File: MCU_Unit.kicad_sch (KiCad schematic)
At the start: 35 parts, among them J401 Solder Holes 4x1 2.54mm 22AWG, J402 Conn_ARM_SWD_TagConnect_TC203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, J403 Solder Wire Pad 1,5x3mm, J404 Solder Wire Pad 1,5x3mm, J405 Solder Wire Pad 1,5x3mm, J406 Solder Wire Pad 1,5x3mm, SW401 KMR232NG ULC, SW402 KMR232NG ULC, SW403 CAS-D20A1, SW404 KMR232NG ULC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

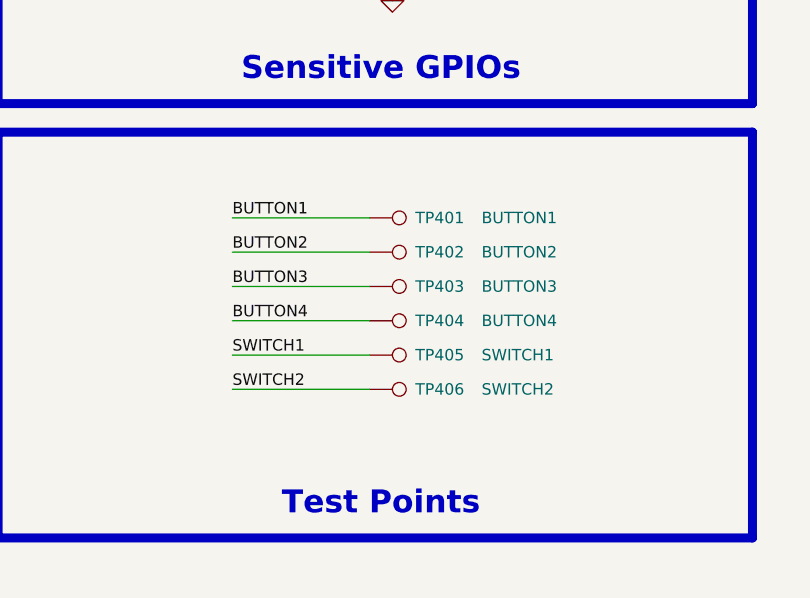
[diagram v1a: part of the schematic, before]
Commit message: Added PCB frame for assembly, almost finished auto-review, only MCU and motors left
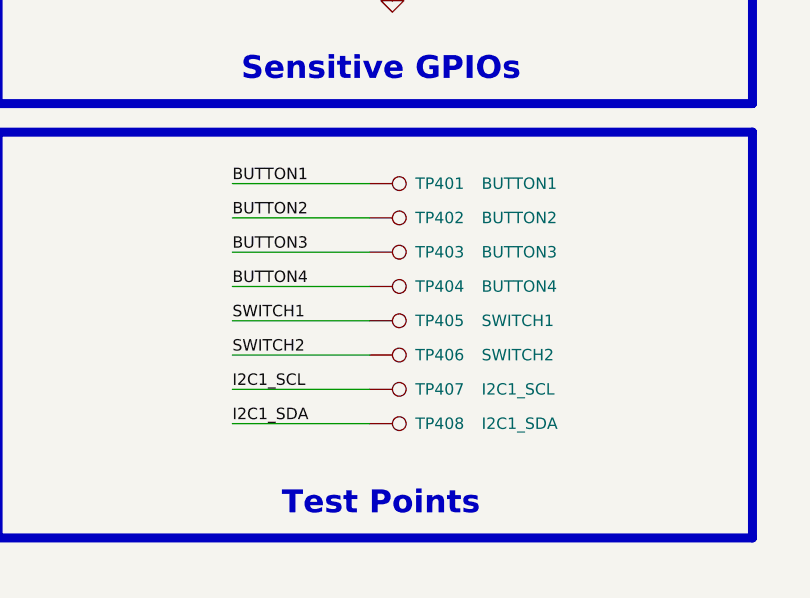
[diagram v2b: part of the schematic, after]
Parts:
- added TP407: I2C1_SCL, 0_Plume:TestPoint_Pad_D0.75mm_Front, symbol Connector:TestPoint
- added TP408: I2C1_SDA, 0_Plume:TestPoint_Pad_D0.75mm_Front, symbol Connector:TestPoint
- TP401, TP402, TP403, TP404, TP405, TP406: footprint 0_Plume:TestPoint_Pad_D0.5mm_Back -> 0_Plume:TestPoint_Pad_D0.5mm_Front
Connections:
- net I2C1_SCL: now also TP407.1
- net I2C1_SDA: now also TP408.1
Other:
- moved on the sheet: TP401, TP402, TP403, TP404, TP405, TP406

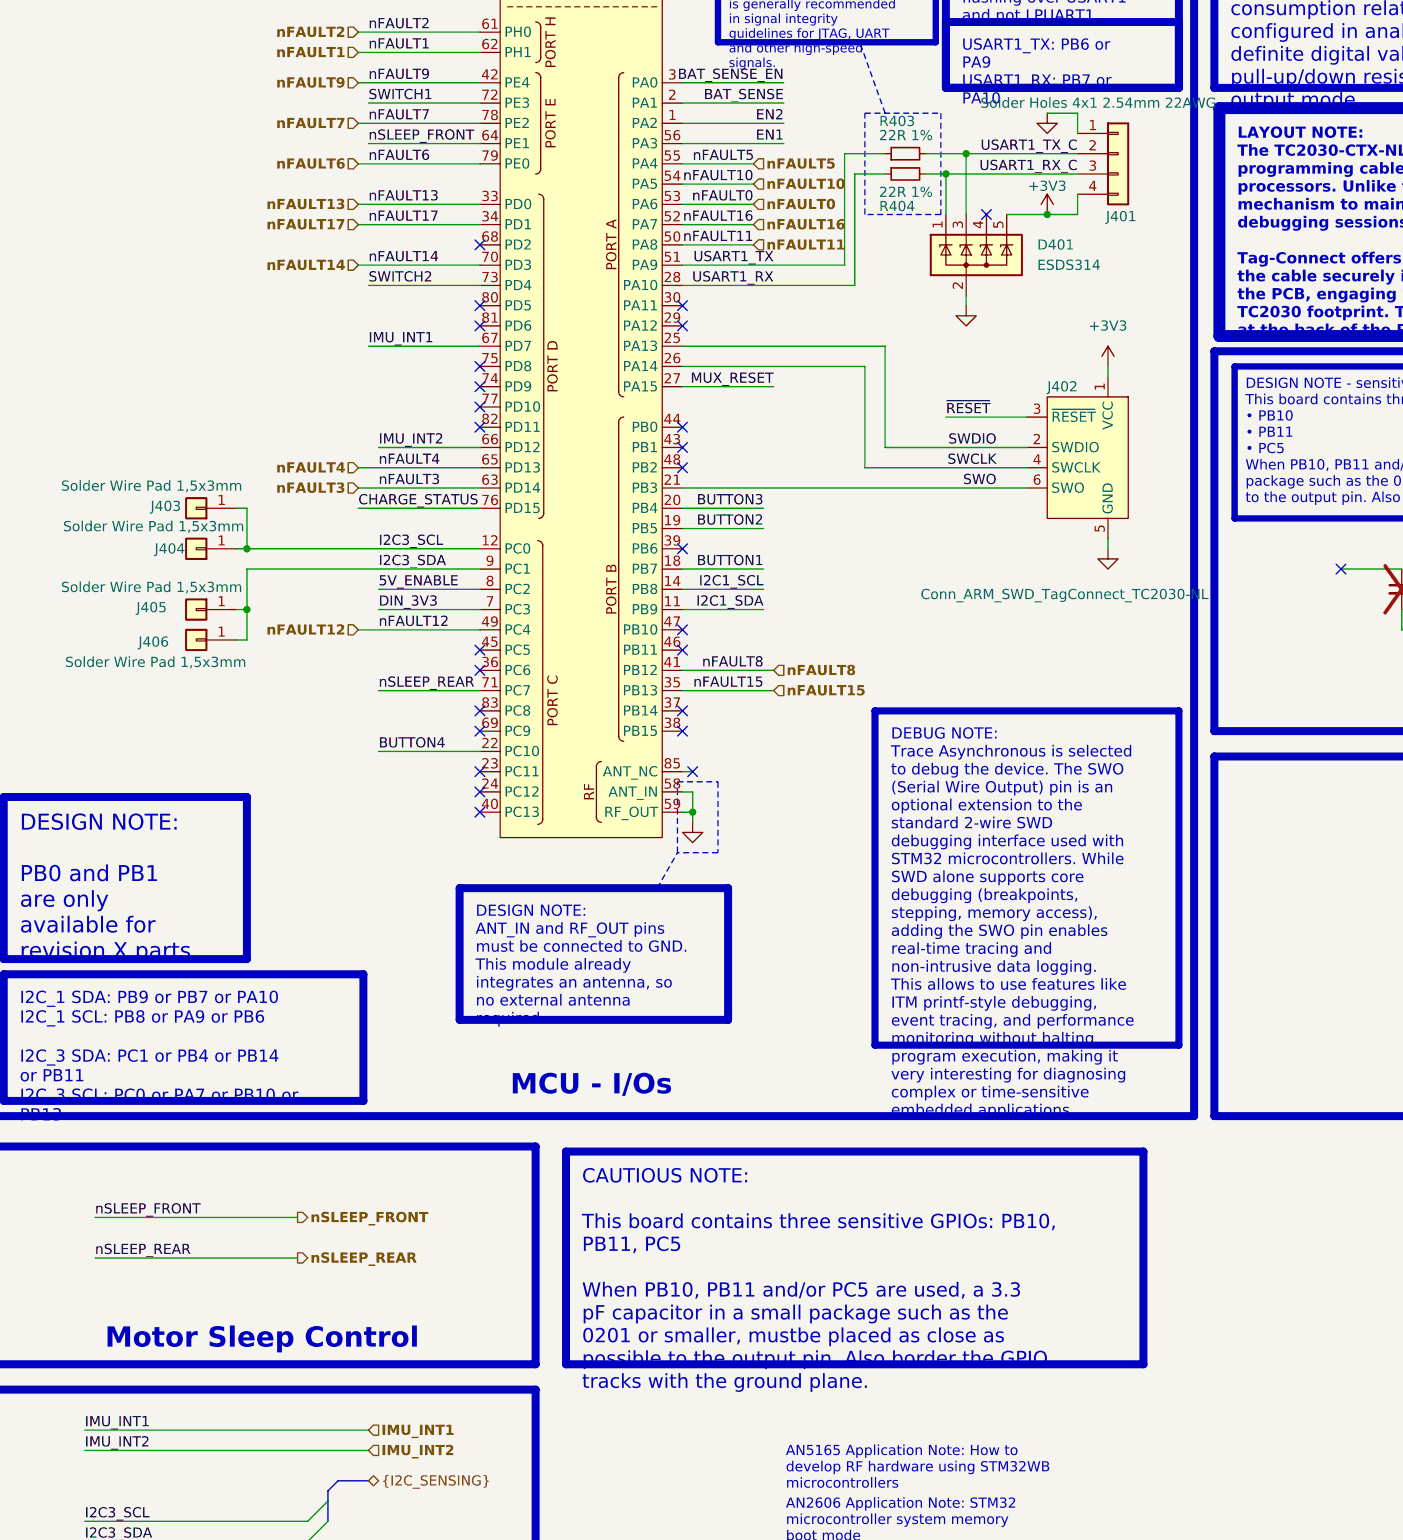
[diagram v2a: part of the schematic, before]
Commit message: Checked everything, corrected footprints, cleaned routing, should be ready to order
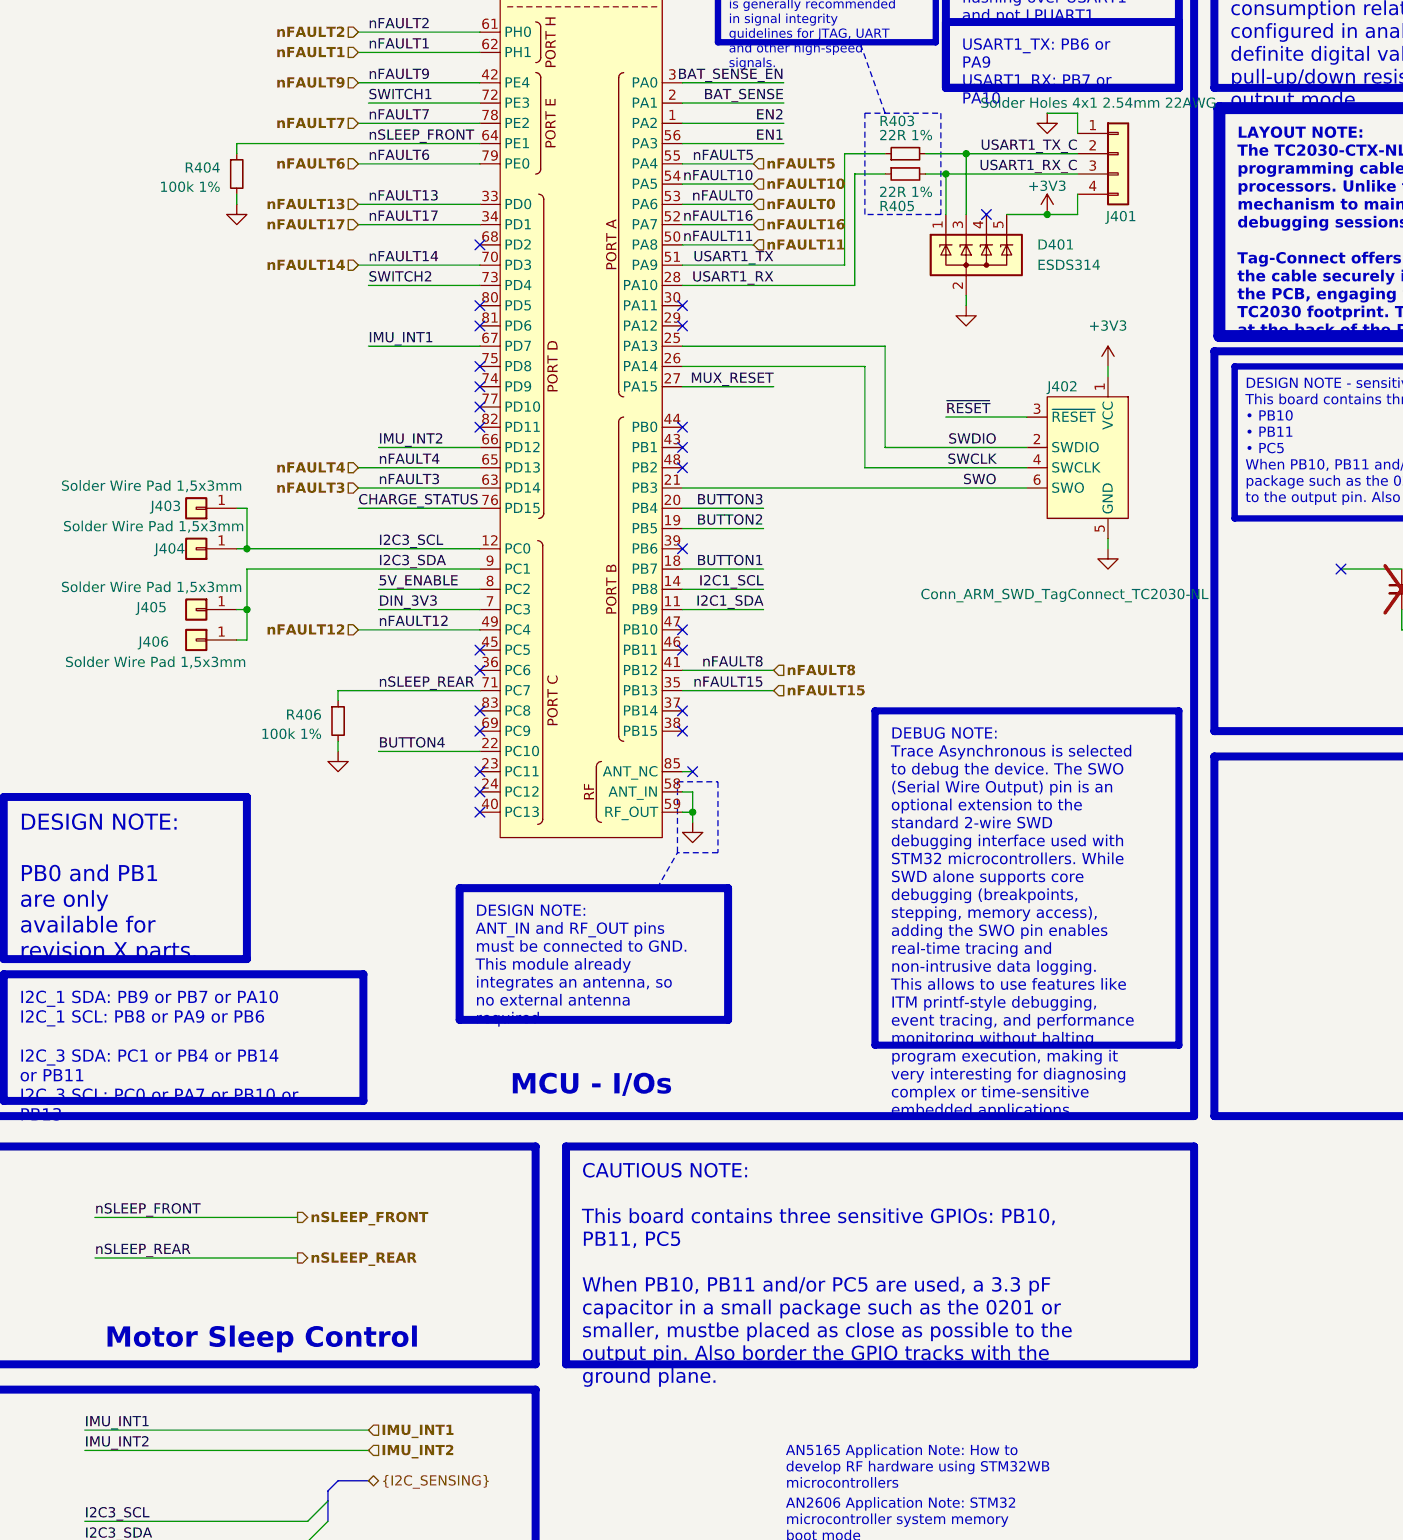
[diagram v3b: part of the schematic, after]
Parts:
- added R404, R406: 100k 1%, Resistor_SMD:R_0402_1005Metric, symbol Device:R_Small
- D401: footprint Package_TO_SOT_SMD:SOT-23-5 -> 0_Plume:SOT-23-5-TEXAS
- U401: footprint RF_Module:ST-SiP-LGA-86-11x7.3mm -> 0_Plume:ST-SiP-LGA-86-11x7.3mm
- renumbered R404 to R405
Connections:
- net GND: now also R404.2, R406.2
- net nSLEEP_FRONT: now also R404.1
- net nSLEEP_REAR: now also R406.1
